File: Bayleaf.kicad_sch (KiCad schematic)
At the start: 71 parts, among them J2 Conn_01x02_Socket, SW1 SW_SPDT, U1 Nice_Nano_V2

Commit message: V1 PCB, confirmed working state
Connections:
- net +BATT: now also SW1.2 (B); no longer SW1.3 (C)
- net RAW: now also SW1.3 (C); no longer SW1.2 (B)
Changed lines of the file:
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@@
 		)
 	)
-	(global_label "RAW"
-		(shape input)
-		(at 133.35 101.6 180)
-		(fields_autoplaced yes)
-		(effects
-			(font
-				(size 1.27 1.27)
-			)
-			(justify right)
-		)
-		(property "Intersheetrefs" "${INTERSHEET_REFS}"
-			(at 126.5548 101.6 0)
-			(effects
-				(font
-					(size 1.27 1.27)
-				)
-				(justify right)
-				(hide yes)
-			)
-		)
-	)
 	(global_label "row-0L"
 		(shape input)
@@
 		)
 	)
+	(global_label "RAW"
+		(shape input)
+		(at 148.59 104.14 0)
+		(fields_autoplaced yes)
+		(effects
+			(font
+				(size 1.27 1.27)
+			)
+			(justify left)
+		)
+		(property "Intersheetrefs" "${INTERSHEET_REFS}"
+			(at 155.3852 104.14 0)
+			(effects
+				(font
+					(size 1.27 1.27)
+				)
+				(justify left)
+				(hide yes)
+			)
+		)
+	)
 	(global_label "row-1L"
 		(shape input)
@@
 	)
 	(symbol
+		(lib_id "power:+BATT")
+		(at 133.35 101.6 90)
+		(unit 1)
+		(exclude_from_sim no)
+		(in_bom yes)
+		(on_board yes)
+		(dnp no)
+		(property "Reference" "#PWR02"
+			(at 137.16 101.6 0)
+			(effects
+				(font
+					(size 1.27 1.27)
+				)
+				(hide yes)
+			)
+		)
+		(property "Value" "+BATT"
+			(at 129.54 101.5999 90)
+			(effects
+				(font
+					(size 1.27 1.27)
+				)
+				(justify left)
+			)
+		)
+		(property "Footprint" ""
+			(at 133.35 101.6 0)
+			(effects
+				(font
+					(size 1.27 1.27)
+				)
+				(hide yes)
+			)
+		)
+		(property "Datasheet" ""
+			(at 133.35 101.6 0)
+			(effects
+				(font
+					(size 1.27 1.27)
+				)
+				(hide yes)
+			)
+		)
+		(property "Description" "Power symbol creates a global label with name \"+BATT\""
+			(at 133.35 101.6 0)
+			(effects
+				(font
+					(size 1.27 1.27)
+				)
+				(hide yes)
+			)
+		)
+		(pin "1"
+		)
+		(instances
+			(project "Bayleaf"
+				(path "/cc4feee6-6309-4a8f-81f1-d1c4eb544ca9"
+					(reference "#PWR02")
+					(unit 1)
+				)
+			)
+		)
+	)
+	(symbol
 		(lib_id "Diode:1N4148W")
 		(at 55.88 157.48 90)
@@
 					(unit 1)
 				)
-			)
-		)
-	)
-	(symbol
-		(lib_id "power:+BATT")
-		(at 148.59 104.14 270)
-		(unit 1)
-		(exclude_from_sim no)
-		(in_bom yes)
-		(on_board yes)
-		(dnp no)
-		(fields_autoplaced yes)
-		(property "Reference" "#PWR02"
-			(at 144.78 104.14 0)
-			(effects
-				(font
-					(size 1.27 1.27)
-				)
-				(hide yes)
-			)
-		)
-		(property "Value" "+BATT"
-			(at 152.4 104.1399 90)
-			(effects
-				(font
-					(size 1.27 1.27)
-				)
-				(justify left)
-			)
-		)
-		(property "Footprint" ""
-			(at 148.59 104.14 0)
-			(effects
-				(font
-					(size 1.27 1.27)
-				)
-				(hide yes)
-			)
-		)
-		(property "Datasheet" ""
-			(at 148.59 104.14 0)
-			(effects
-				(font
-					(size 1.27 1.27)
-				)
-				(hide yes)
-			)
-		)
-		(property "Description" "Power symbol creates a global label with name \"+BATT\""
-			(at 148.59 104.14 0)
-			(effects
-				(font
-					(size 1.27 1.27)
-				)
-				(hide yes)
-			)
-		)
-		(pin "1"
-		)
-		(instances
-			(project ""
-				(path "/cc4feee6-6309-4a8f-81f1-d1c4eb544ca9"
-					(reference "#PWR02")
-					(unit 1)
-				)

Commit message: renamed schematic refs
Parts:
- L_U1: renamed from U1; value Nice_Nano_V2 -> N!N_V2
- renumbered D1 to L_D1, D10 to L_D10, D11 to L_D11, D12 to L_D12, D13 to L_D13, D14 to L_D14, D15 to L_D15, D16 to L_D16, D17 to L_D17, D18 to L_D18, D19 to L_D19, D2 to L_D2, D20 to L_D20, D21 to L_D21, D22 to L_D22, D23 to L_D23, D24 to L_D24, D25 to L_D25, D26 to L_D26, D27 to L_D27, D28 to L_D28, D29 to L_D29, D3 to L_D3, D30 to L_D30, D4 to L_D4, D5 to L_D5, D6 to L_D6, D7 to L_D7, D8 to L_D8, D9 to L_D9, H1 to L_H1, H2 to L_H2, H3 to L_H3, H4 to L_H4, H5 to L_H5, H6 to L_H6, H7 to L_H7, J2 to L_J2, RSW1 to L_RSW1, S1 to L_S1, S10 to L_S10, S11 to L_S11, S12 to L_S12, S13 to L_S13, S14 to L_S14, S15 to L_S15, S16 to L_S16, S17 to L_S17, S18 to L_S18, S19 to L_S19, S2 to L_S2, S20 to L_S20, S21 to L_S21, S22 to L_S22, S23 to L_S23, S24 to L_S24, S25 to L_S25, S26 to L_S26, S27 to L_S27, S28 to L_S28, S29 to L_S29, S3 to L_S3, S30 to L_S30, S4 to L_S4, S5 to L_S5, S6 to L_S6, S7 to L_S7, S8 to L_S8, S9 to L_S9, SW1 to L_SW1
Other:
- moved on the sheet: L_H1, L_H2, L_H3, L_H4, L_H5, L_H6, L_H7, L_J2, L_RSW1, L_SW1, L_U1

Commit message: draft split labels schematic
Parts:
- added R_D1, R_D10, R_D11, R_D12, R_D13, R_D14, R_D15, R_D16, R_D17, R_D18, R_D19, R_D2, R_D20, R_D21, R_D22, R_D23, R_D24, R_D25, R_D26, R_D27, R_D28, R_D29, R_D3, R_D30, R_D4, R_D5, R_D6, R_D7, R_D8, R_D9: 1N4148W, Diode_SMD:D_SOD-123, symbol Diode:1N4148W
- added R_H1, R_H2, R_H3, R_H4, R_H5, R_H6, R_H7: MountingHole, MountingHole:MountingHole_2.2mm_M2, symbol Mechanical:MountingHole
- added R_J1: Conn_01x02_Socket, Connector_JST:JST_SH_SM02B-SRSS-TB_1x02-1MP_P1.00mm_Horizontal, symbol Connector:Conn_01x02_Socket
- added R_RSW1: SW_RST, Button_Switch_SMD:SW_Tactile_SPST_NO_Straight_CK_PTS636Sx25SMTRLFS, symbol Lily58_Pro-rescue:SW_RST-Lily58-cache
- added R_S1, R_S10, R_S11, R_S12, R_S13, R_S14, R_S15, R_S16, R_S17, R_S18, R_S19, R_S2, R_S20, R_S21, R_S22, R_S23, R_S24, R_S25, R_S26, R_S27, R_S28, R_S29, R_S3, R_S30, R_S4, R_S5, R_S6, R_S7, R_S8, R_S9: Keyswitch, Bayleaf:CPG1316S01D02_mikeholscher, symbol ScottoKeebs:Placeholder_Keyswitch
- added R_SW1: SW_SPDT, Button_Switch_SMD:SW_SPDT_PCM12, symbol Switch:SW_SPDT
- added R_U2: N!N_V2, ScottoKeebs_MCU:Nice_Nano_V2, symbol ScottoKeebs:MCU_Nice_Nano_V2
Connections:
- net +BATT: now also R_J1.1 (Pin_1), R_SW1.2 (B); no longer L_J2.1 (Pin_1), L_SW1.2 (B)
- net GND renamed GND_L
- net RAW renamed RAW_L
- net RESET renamed RESET_L
- net VCC renamed VCC_L
- new net: R_D7.2 (A), R_S7.2
- new net: R_D23.2 (A), R_S23.2
- new net: R_D10.2 (A), R_S10.2
- new net: R_D26.2 (A), R_S26.2
- new net: R_D30.2 (A), R_S30.2
- new net: R_D3.2 (A), R_S3.2
- new net: R_D18.2 (A), R_S18.2
- new net: R_D12.2 (A), R_S12.2
- new net: R_D8.2 (A), R_S8.2
- new net: R_D19.2 (A), R_S19.2
- new net: R_D25.2 (A), R_S25.2
- new net: R_D13.2 (A), R_S13.2
- new net: R_D22.2 (A), R_S22.2
- new net: R_D6.2 (A), R_S6.2
- new net: R_D16.2 (A), R_S16.2
- new net: R_D4.2 (A), R_S4.2
- new net: R_D29.2 (A), R_S29.2
- new net: R_D15.2 (A), R_S15.2
- new net: R_D28.2 (A), R_S28.2
- new net: R_D17.2 (A), R_S17.2
- new net: R_D5.2 (A), R_S5.2
- new net: R_D27.2 (A), R_S27.2
- new net: R_D24.2 (A), R_S24.2
- new net: R_D1.2 (A), R_S1.2
- new net: R_D14.2 (A), R_S14.2
- new net: R_D2.2 (A), R_S2.2
- new net: R_D21.2 (A), R_S21.2
- new net: R_D9.2 (A), R_S9.2
- new net: R_D20.2 (A), R_S20.2
- new net: R_D11.2 (A), R_S11.2
- new net +BATT_L: L_J2.1 (Pin_1), L_SW1.2 (B)
- new net GND_R: R_J1.2 (Pin_2), R_RSW1.1, R_U2.23 (GND), R_U2.3 (GND), R_U2.4 (GND)
- new net RAW_R: R_SW1.3 (C), R_U2.24 (B+)
- new net RESET_R: R_RSW1.2, R_U2.22 (RST)
- new net VCC_R: R_U2.21 (3.3v)
- new net col-0R: R_S1.1, R_S13.1, R_S19.1, R_S25.1, R_S7.1, R_U2.5 (2)
- new net col-1R: R_S14.1, R_S2.1, R_S20.1, R_S26.1, R_S8.1, R_U2.6 (3)
- new net col-2R: R_S15.1, R_S21.1, R_S27.1, R_S3.1, R_S9.1, R_U2.7 (4)
- new net col-3R: R_S10.1, R_S16.1, R_S22.1, R_S28.1, R_S4.1, R_U2.8 (5)
- new net col-4R: R_S11.1, R_S17.1, R_S23.1, R_S29.1, R_S5.1, R_U2.9 (6)
- new net col-5R: R_S12.1, R_S18.1, R_S24.1, R_S30.1, R_S6.1, R_U2.10 (7)
- new net row-0R: R_D1.1 (K), R_D2.1 (K), R_D3.1 (K), R_D4.1 (K), R_D5.1 (K), R_D6.1 (K), R_U2.20 (21)
- new net row-1R: R_D10.1 (K), R_D11.1 (K), R_D12.1 (K), R_D7.1 (K), R_D8.1 (K), R_D9.1 (K), R_U2.19 (20)
- new net row-2R: R_D13.1 (K), R_D14.1 (K), R_D15.1 (K), R_D16.1 (K), R_D17.1 (K), R_D18.1 (K), R_U2.18 (19)
- new net row-3R: R_D19.1 (K), R_D20.1 (K), R_D21.1 (K), R_D22.1 (K), R_D23.1 (K), R_D24.1 (K), R_U2.17 (18)
- new net row-4R: R_D25.1 (K), R_D26.1 (K), R_D27.1 (K), R_D28.1 (K), R_D29.1 (K), R_D30.1 (K), R_U2.16 (15)
- no-connect marks 1 -> 2

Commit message: ref checkpoint
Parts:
- renumbered R_U2 to R_U1
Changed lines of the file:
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@@
 		(dnp no)
 		(fields_autoplaced yes)
-		(property "Reference" "R_U2"
+		(property "Reference" "R_U1"
 			(at 232.41 207.01 0)
 			(effects
@@
 			(project "Bayleaf"
 				(path "/cc4feee6-6309-4a8f-81f1-d1c4eb544ca9"
-					(reference "R_U2")
+					(reference "R_U1")
 					(unit 1)
 				)

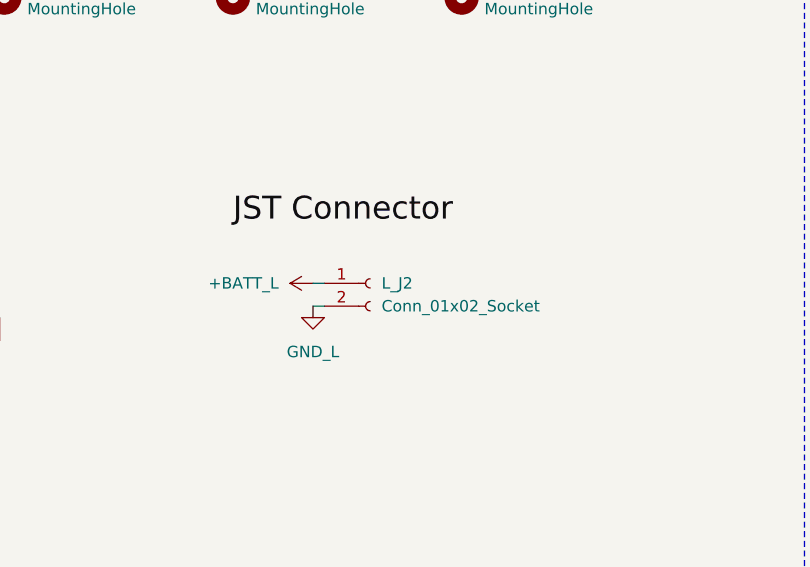
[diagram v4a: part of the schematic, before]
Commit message: fix v-score + edge zone fill fix
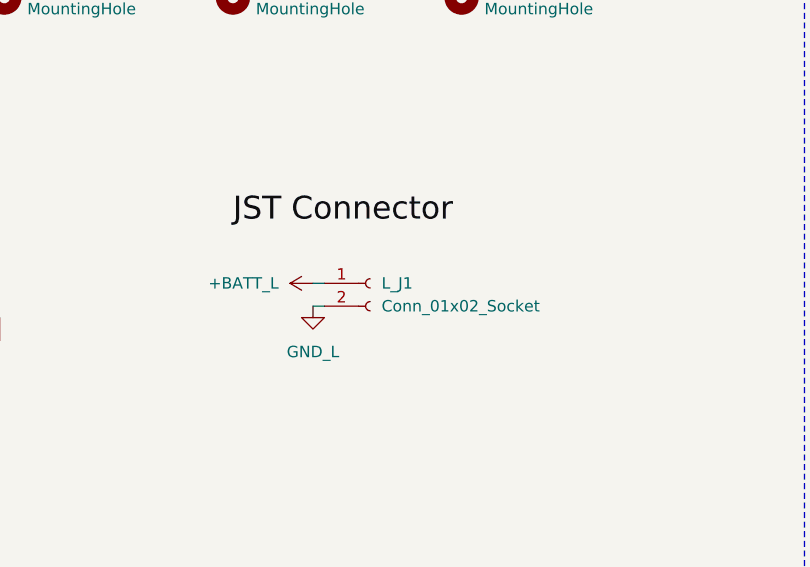
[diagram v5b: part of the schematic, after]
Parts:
- renumbered L_J2 to L_J1
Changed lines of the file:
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@@
 		(dnp no)
 		(fields_autoplaced yes)
-		(property "Reference" "L_J2"
+		(property "Reference" "L_J1"
 			(at 143.51 247.6499 0)
 			(effects
@@
 			(project "Bayleaf"
 				(path "/cc4feee6-6309-4a8f-81f1-d1c4eb544ca9"
-					(reference "L_J2")
+					(reference "L_J1")
 					(unit 1)
 				)
